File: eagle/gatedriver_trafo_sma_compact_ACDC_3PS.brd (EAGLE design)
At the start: 128.5 x 101.9 mm, 14 parts

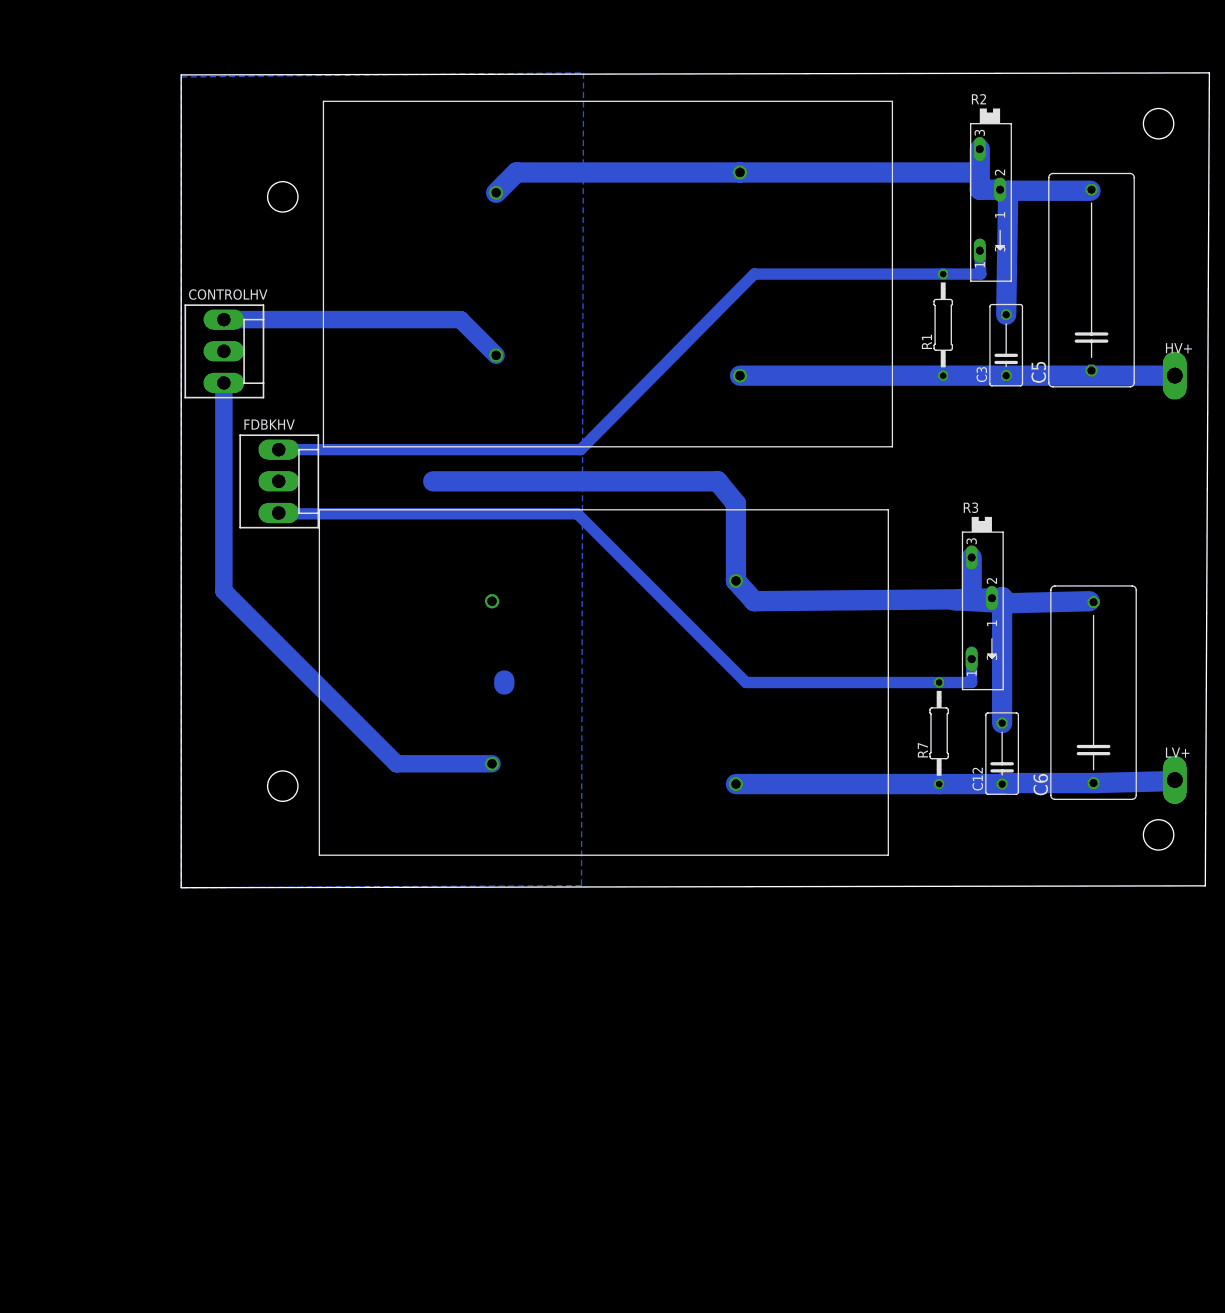
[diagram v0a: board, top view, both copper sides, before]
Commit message: 3PS, 2 1kV in parallel
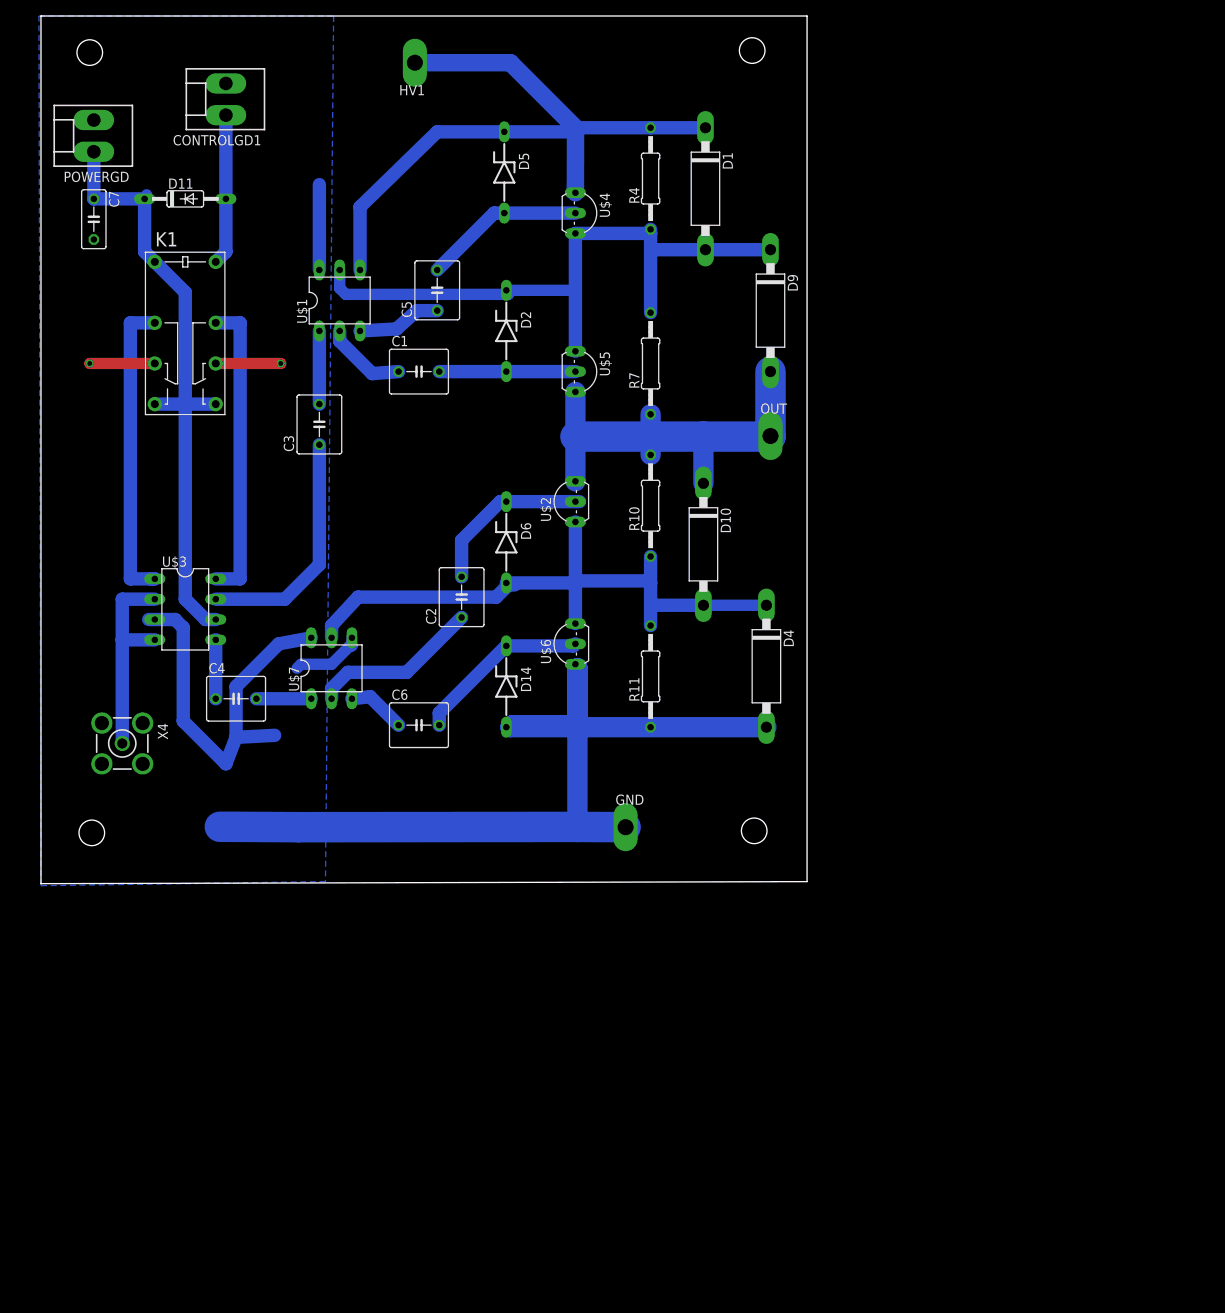
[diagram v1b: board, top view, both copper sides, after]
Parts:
- removed C12: .01u, rcl:C075-042X103
- removed CONTROLHV, FDBKHV: (no value), con-molex:KK-156-3
- removed HV+, LV+: TPPAD1-20Y, testpad:P1-20Y
- removed R1: 2M, resistor:0207/12
- removed R2, R3: (no value), pot:SP19L
- added C1, C2, C4: (no value), resistor:C050-055X075
- added C7: (no value), rcl:C050-030X075
- added CONTROLGD1, POWERGD: (no value), con-molex:KK-156-2
- added D1, D10, D4, D9: P6KEXXA, diode:C1702-15
- added D11: 1N4148DO35-10, diode:DO35-10
- added D14, D2, D5, D6: 4742, diode:ZDIO-10
- added GND, HV1, OUT: TPPAD1-20Y, testpad:P1-20Y
- added K1: G5V-2, relay:G5V-2
- added R10, R11, R4: 10M, rcl:0207/12
- added U$3: UCC27425, texas:DIL08
- added U$4, U$5: VP0550, transistor-fet:TO92-
- added U$6: VN0550, transistor-fet:TO92-
- added U$7: DA-2320, trafo:DIL06
- added X4: BU-SMA-V, con-coax:BU-SMA-V
- C3: value .01u -> (none); device rcl:C075-042X103 -> resistor:C050-055X075
- C5, C6: value 1u -> (none); device rcl:C225-108X268 -> resistor:C050-055X075
- R7: value 2M -> 10M; device resistor:0207/12 -> rcl:0207/12
- U$1: value EMCO-F104PIN -> DA-2320; device dc-dc-converter:EMCO-F -> trafo:DIL06
- U$2: value EMCO-F104PIN -> VN0550; device dc-dc-converter:EMCO-F -> transistor-fet:TO92-
- moved C3 86.4 mm to (35.1, 57.7)
- moved C6 84.4 mm to (47.5, 20.1), turned to 0 degrees
- moved C5 81.8 mm to (49.8, 74.4)
- moved R7 58.6 mm to (76.5, 65.3)
- moved U$2 34.4 mm to (67.1, 48.0), turned to 90 degrees
- moved U$1 20.7 mm to (37.6, 73.2)
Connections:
- removed net N$8: FDBKHV.3, R3.A, R7.2
- new net +15V: C7.1, D11.C, K1.1, K1.8, K1.9, POWERGD.1, U$3.6
- new net ENSW: CONTROLGD1.1, D11.A, K1.16
- new net N$11: C1.2, D2.A, U$5.2
- new net N$13: D10.A, D4.C, D6.A, R10.1, R11.2, U$2.3, U$6.1
- new net N$14: K1.4, U$3.1
- new net N$15: K1.13, U$3.8
- new net N$16: C5.2, D5.A, U$4.2
- new net N$17: D1.C, D5.C, HV1.TP, R4.2, U$1.4, U$4.3
- new net N$18: D1.A, D2.C, D9.C, R4.1, R7.2, U$1.5, U$4.1, U$5.3
- new net N$21: D10.C, D9.A, OUT.TP, R10.2, R7.1, U$2.1, U$5.1
- new net N$22: C2.1, U$7.2
- new net N$23: C6.1, U$7.3
- new net N$25: C2.2, D6.C, U$2.2
- new net N$27: C6.2, D14.C, U$6.2
- new net N$6: C4.2, U$7.1
- new net N$7: C5.1, U$1.3
- new net N$9: U$7.5
- net GND: now also C7.2, CONTROLGD1.2, D14.A, D4.A, GND.TP, K1.11, K1.6, POWERGD.2, R11.1, U$1.6, U$3.3, U$6.3, U$7.4, U$7.6, X4.2, X4.3, X4.4, X4.5; no longer C12.2, C3.2, C5.2, C6.2, CONTROLHV.2, FDBKHV.2, R2.E, R2.S, R3.E, R3.S, U$1.P$2, U$1.P$4, U$2.P$2, U$2.P$4
- net N$1: now also U$3.2, U$3.4, X4.1; no longer C3.1, C5.1, HV+.TP, R1.1, U$1.P$3
- net N$2: now also C3.1, U$3.7; no longer C12.1, C6.1, LV+.TP, R7.1, U$2.P$3
- net N$3: now also C3.2, U$1.1; no longer FDBKHV.1, R1.2, R2.A
- net N$4: now also C4.1, U$3.5; no longer CONTROLHV.1, U$1.P$1
- net N$5: now also C1.1, U$1.2; no longer CONTROLHV.3, U$2.P$1
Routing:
- net N$8: track 99.5 -> 0.00 mm
- net N$17: track 0.00 -> 94.8 mm
- net N$3: track 99.8 -> 9.14 mm
- net N$18: track 0.00 -> 82.5 mm
- net +15V: track 0.00 -> 77.6 mm
- net N$5: track 68.5 -> 10.3 mm
- net N$13: track 0.00 -> 55.6 mm
- net N$21: track 0.00 -> 54.6 mm
- net N$14: track 0.00 -> 38.6 mm
- net N$15: track 0.00 -> 38.1 mm
- net N$4: track 35.9 -> 7.37 mm
- net N$1: track 54.4 -> 26.2 mm
- net N$9: track 0.00 -> 26.6 mm
- net N$2: track 55.0 -> 29.7 mm
- net N$27: track 0.00 -> 22.1 mm
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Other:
- board size 128.5 x 101.9 mm -> 95.8 x 108.5 mm

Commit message: IXYS board solution, gatedriver components
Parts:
- added C8: (no value), resistor:C102-064X133
- added R1, R12, R2, R3, R5, R6, R8, R9: 1M, rcl:0207/10
- added R13, R14: 1M, rcl:0207/12
- R10, R11, R4, R7: value 10M -> 1M; device rcl:0207/12 -> rcl:0207/10
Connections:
- new net N$10: C1.2, D2.A, R6.1
- new net N$12: R2.1, R8.2, U$4.2
- new net N$19: C3.2, R13.2
- new net N$20: C4.2, R14.2
- new net N$8: R1.1, R6.2, U$5.2
- net GND: now also C8.2
- net N$11: now also R12.2, R5.1, U$6.2; no longer C1.2, D2.A, U$5.2
- net N$16: now also R8.1; no longer U$4.2
- net N$17: now also C8.1, R2.2
- net N$18: now also R1.2
- net N$25: now also R3.1, R9.1, R9.2
- net N$27: now also R12.1; no longer U$6.2
- net N$3: now also R13.1; no longer C3.2
- net N$6: now also R14.1; no longer C4.2
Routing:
- net N$27: track 22.1 -> 1.52 mm
- net N$11: track 17.0 -> 0.00 mm
- net N$3: track 9.14 -> 0.00 mm
- net N$16: track 20.2 -> 11.3 mm
- net N$6: track 6.86 -> 0.00 mm
- net N$21: track 54.6 -> 57.1 mm
- net N$18: track 82.5 -> 85.1 mm
- net N$13: track 55.6 -> 58.1 mm
